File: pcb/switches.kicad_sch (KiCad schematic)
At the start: 8 parts, among them U2 SN74LVC245APW, U3 SN74LVC245APW

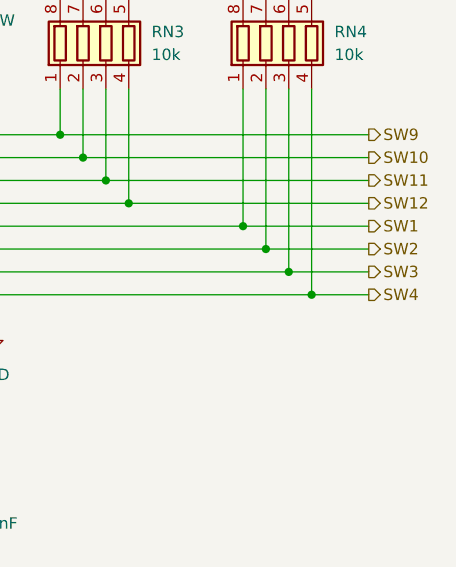
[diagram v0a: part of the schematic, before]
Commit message: fixes #18 fixes #26
replace usb-c connector
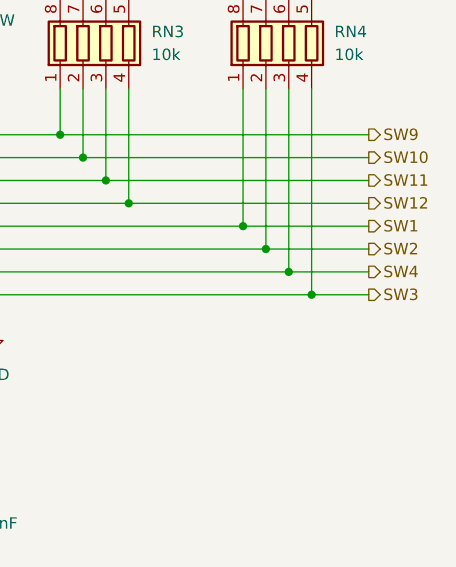
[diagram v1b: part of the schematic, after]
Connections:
- net SW3: now also RN4.4 (R4.1), U3.11 (B8); no longer RN4.3 (R3.1), U3.12 (B7)
- net SW4: now also RN4.3 (R3.1), U3.12 (B7); no longer RN4.4 (R4.1), U3.11 (B8)
